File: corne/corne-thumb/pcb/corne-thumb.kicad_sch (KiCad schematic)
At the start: 91 parts, among them J1 MJ-4PP-9, J2 OLED, J6 MJ-4PP-9, J7 OLED, SW1 SW_PUSH, SW10 SW_PUSH, SW11 SW_PUSH, SW12 SW_PUSH, SW13 SW_PUSH, SW14 SW_PUSH, SW15 SW_PUSH, SW16 SW_PUSH, SW17 SW_PUSH, SW18 SW_PUSH, SW19 SW_PUSH, SW2 SW_PUSH, SW20 SW_PUSH, SW21 SW_PUSH, SW22 SW_PUSH, SW23 SW_PUSH, SW24 SW_PUSH, SW25 SW_PUSH, SW26 SW_PUSH, SW27 SW_PUSH, SW28 SW_PUSH, SW29 SW_PUSH, SW3 SW_PUSH, SW30 SW_PUSH, SW31 SW_PUSH, SW32 SW_PUSH, SW33 SW_PUSH, SW34 SW_PUSH, SW35 SW_PUSH, SW36 SW_PUSH, SW37 SW_PUSH, SW38 SW_PUSH, SW39 SW_PUSH, SW4 SW_PUSH, SW41 SW_PUSH, SW42 SW_PUSH, SW5 SW_PUSH, SW6 SW_PUSH, SW7 SW_PUSH, SW8 SW_PUSH, SW9 SW_PUSH, U1 ProMicro, U2 ProMicro

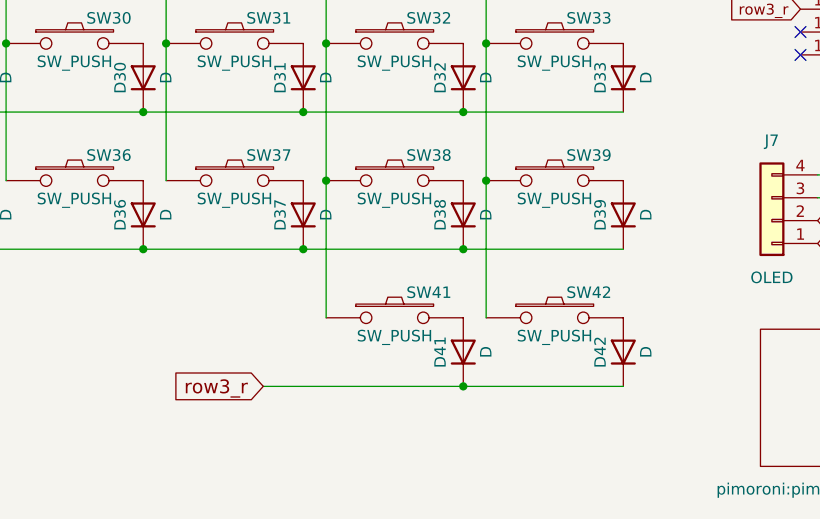
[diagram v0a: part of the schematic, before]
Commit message: corne/thumb: move thumb trackball to the 42nd key position
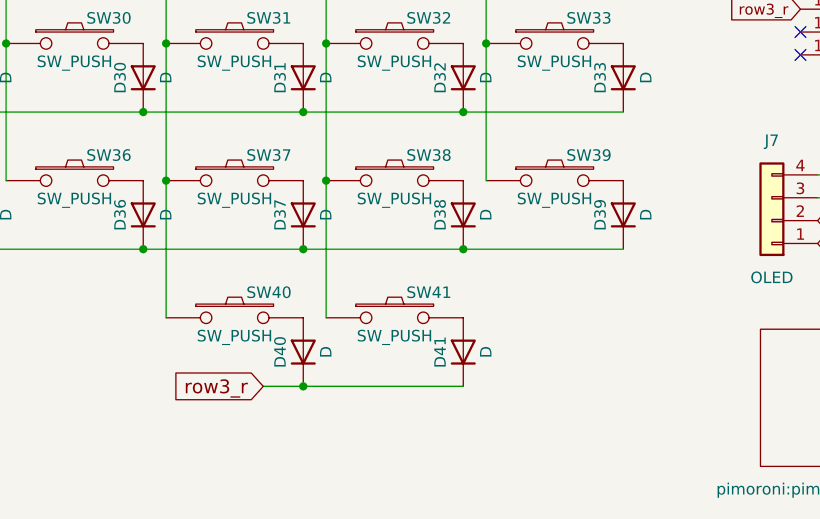
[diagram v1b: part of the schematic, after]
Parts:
- removed D42: D, kbd:D3_TH, symbol Device:D
- removed SW42: SW_PUSH, kbd:CherryMX_ChocV2_1.5u, symbol corne-light-rescue:SW_PUSH-kbd
- added D40: D, kbd:D3_TH, symbol Device:D
- added SW40: SW_PUSH, kbd:CherryMX_ChocV2_1u, symbol corne-light-rescue:SW_PUSH-kbd
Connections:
- net col3_r: now also SW40.1
- net row3_r: now also D40.1 (K)
- new net: D40.2 (A), SW40.2
